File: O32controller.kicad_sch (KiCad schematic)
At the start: 42 parts, among them J1 SWD, J10 3V3, J11 GND, J12 I2C/RS485_2, J2 BATT+, J3 BATT-, J7 BATT+, J8 BATT-, J9 I2C/RS485_1, SW1 RESET, U1 MA702GQ-P, U2 STSPIN32F0A, U3 THVD1420DRLR

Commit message: silkscreen pretty much done
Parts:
- C9: MP (none) -> EEE-FN1E101UP
- J10, J11: now left out of the parts list
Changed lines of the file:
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@@
       (effects (font (size 1.27 1.27)) hide)
     )
-    (property "Datasheet" "~" (id 3) (at 226.06 31.75 0)
+    (property "Datasheet" "https://www.digikey.com/en/products/detail/panasonic-electronic-components/EEE-FN1E101UP/11656944" (id 3) (at 226.06 31.75 0)
+      (effects (font (size 1.27 1.27)) hide)
+    )
+    (property "MP" "EEE-FN1E101UP" (id 4) (at 226.06 31.75 0)
       (effects (font (size 1.27 1.27)) hide)
     )
@@
   )
   (symbol (lib_id "Connector_Generic:Conn_01x01") (at 261.62 148.59 0) (unit 1)
-    (in_bom yes) (on_board yes) (fields_autoplaced)
+    (in_bom no) (on_board yes) (fields_autoplaced)
     (property "Reference" "J10" (id 0) (at 264.16 147.3199 0)
       (effects (font (size 1.27 1.27)) (justify left))
@@
   )
   (symbol (lib_id "Connector_Generic:Conn_01x01") (at 261.62 153.67 0) (unit 1)
-    (in_bom yes) (on_board yes) (fields_autoplaced)
+    (in_bom no) (on_board yes) (fields_autoplaced)
     (property "Reference" "J11" (id 0) (at 264.16 152.3999 0)
       (effects (font (size 1.27 1.27)) (justify left))

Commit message: finish, generate gerbers
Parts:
- added C21: 1nF, Capacitor_SMD:C_0402_1005Metric, symbol Device:C_Small
- C1, C4, C5, C6, C7: MP (none) -> CL05A104KA5NNNC
- C10: MP (none) -> GCM155C71A105KE38D
- C11: MP (none) -> CC0402MRX7R9BB102
- C8: MP (none) -> EEE-FN1E101UP
- D1, D5, D6: MP (none) -> SDM2U30CSP
- D2: MP (none) -> ESDA17P20-1F2
- J1: MP (none) -> SM04B-SRSS-TB(LF)(SN)
- L1: MP (none) -> VLS201612CX-220M-1
- R14, R17, R20: MP (none) -> RC0402FR-072K2L
- R22: MP (none) -> RC0402FR-07121KL
- R26: value 40k -> 41.2k; MP (none) -> RC0402FR-0741K2L
- R27: MP (none) -> RC0402FR-0710KL
- R28, R29: MP (none) -> RC0402FR-071KL
- SW1: MP (none) -> EVQ-P7A01P
- TP2: now left out of the parts list
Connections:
- net BUS_SENSE: now also C21.1
- net GND: now also C21.2

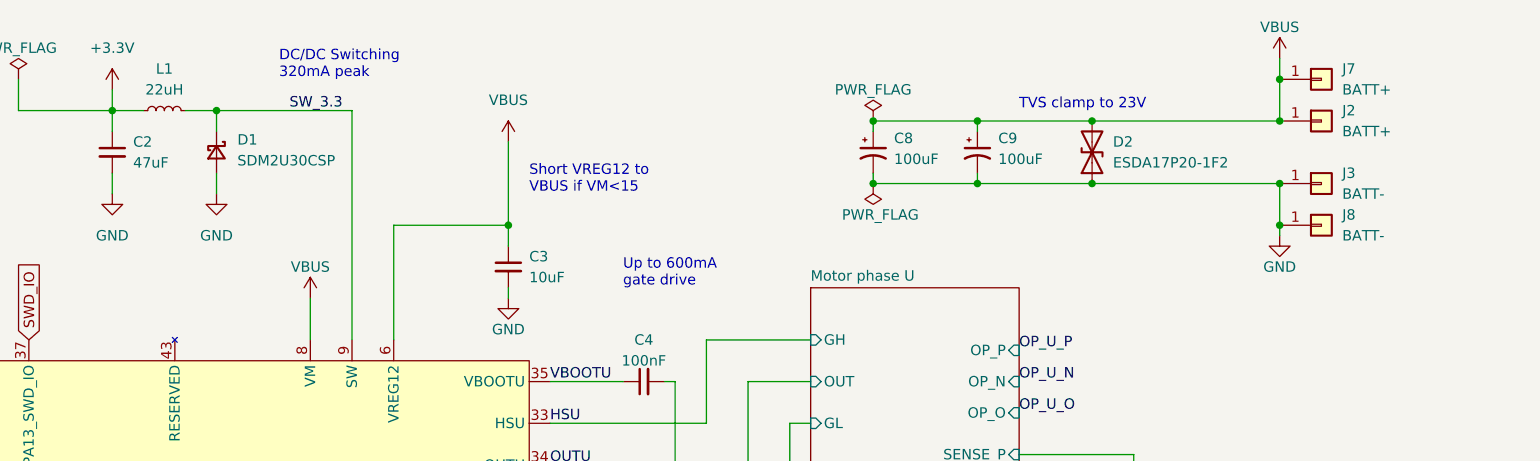
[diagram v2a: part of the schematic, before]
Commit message: clean up v2, fix libraries, netties, fix TVS dir
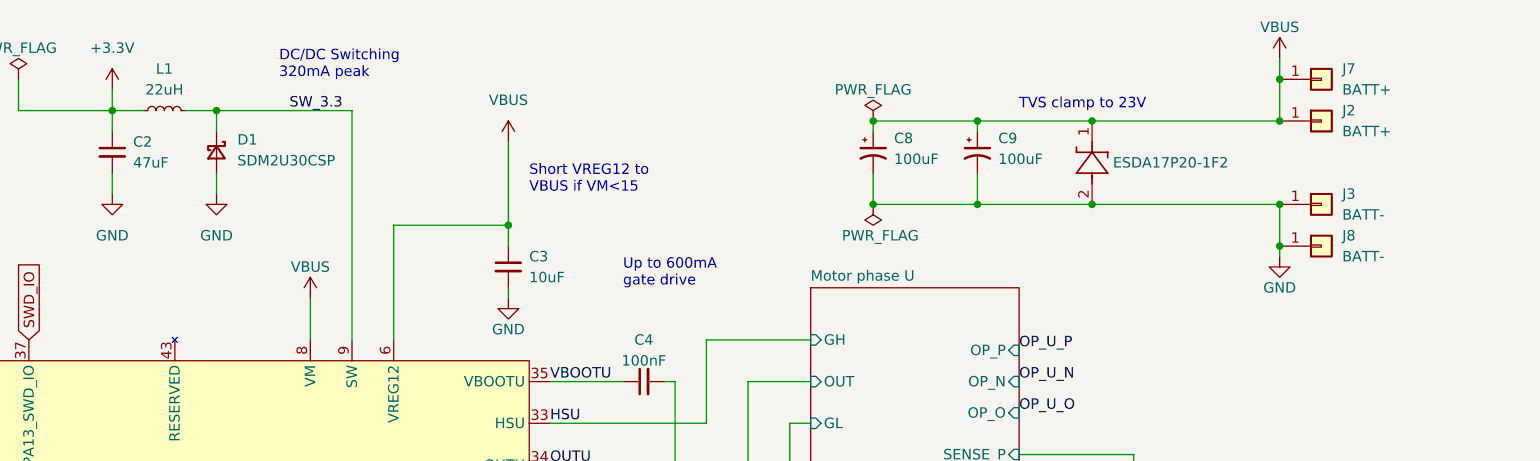
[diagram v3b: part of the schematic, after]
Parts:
- removed D2: ESDA17P20-1F2, Diode_SMD:D_0402_CSP, symbol Device:D_TVS
- added CR1: ESDA17P20-1F2, O32controller:SMT2_0P91X0P63_STM-L, symbol O32controller:ESDA17P20-1F2
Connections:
- net GND: now also CR1.2
- net VBUS: now also CR1.1
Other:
- moved on the sheet: J3, J8

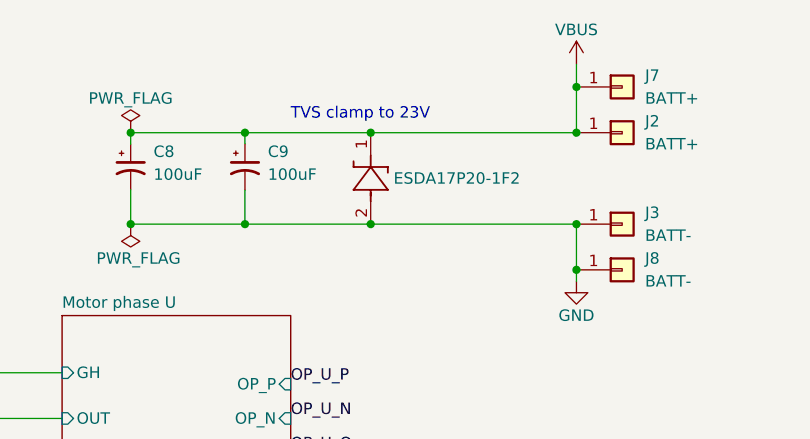
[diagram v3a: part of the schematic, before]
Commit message: remove motor conn from ibom, reannotate tvs diode
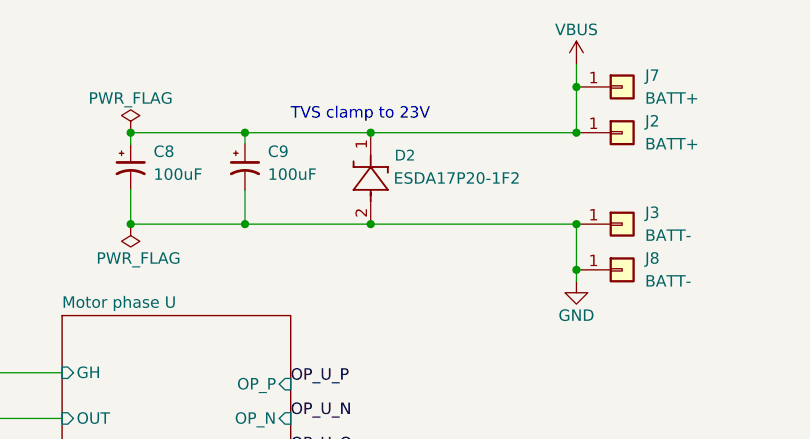
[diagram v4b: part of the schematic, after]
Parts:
- D2: renamed from CR1; MP (none) -> ESDA17P20-1F2
- NT4, NT5: footprint NetTie:NetTie-small -> O32controller:NetTie-2_SMD_Pad0.25mm
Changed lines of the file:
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@@
   (symbol (lib_id "O32controller:ESDA17P20-1F2") (at 240.03 38.1 90) (unit 1)
     (in_bom yes) (on_board yes) (dnp no)
-    (property "Reference" "CR1" (at 232.41 33.02 0)
-      (effects (font (size 1.524 1.524)) hide)
+    (property "Reference" "D2" (at 243.84 30.48 90)
+      (effects (font (size 1.2 1.2)))
     )
     (property "Value" "ESDA17P20-1F2" (at 242.57 33.02 90)
@@
       (effects (font (size 1.27 1.27) italic) hide)
     )
-    (property "Datasheet" "ESDA17P20-1F2" (at 247.65 38.1 0)
+    (property "Datasheet" "https://www.st.com/resource/en/datasheet/esda17p20-1f2.pdf" (at 247.65 38.1 0)
       (effects (font (size 1.27 1.27) italic) hide)
     )
-    (pin "1")
-    (pin "2")
-    (instances
-      (project "O32controller"
-        (path "/af2b7c4e-7b6b-40c8-b9a1-0c412d67fa31"
-          (reference "CR1") (unit 1)
+    (property "MP" "ESDA17P20-1F2" (at 240.03 38.1 90)
+      (effects (font (size 1.27 1.27)) hide)
+    )
+    (pin "1")
+    (pin "2")
+    (instances
+      (project "O32controller"
+        (path "/af2b7c4e-7b6b-40c8-b9a1-0c412d67fa31"
+          (reference "D2") (unit 1)
         )
       )
@@
       (effects (font (size 1.27 1.27)))
     )
-    (property "Footprint" "NetTie:NetTie-small" (at 88.9 171.45 0)
+    (property "Footprint" "O32controller:NetTie-2_SMD_Pad0.25mm" (at 88.9 171.45 0)
       (effects (font (size 1.27 1.27)) hide)
     )
@@
       (effects (font (size 1.27 1.27)))
     )
-    (property "Footprint" "NetTie:NetTie-small" (at 111.76 171.45 0)
-      (effects (font (size 1.27 1.27)) hide)
-    )
+    (property "Footprint" "O32controller:NetTie-2_SMD_Pad0.25mm" (at 111.76 171.45 0)
+      (effects (font (size 1.27 1.27)) hide)
+    )
